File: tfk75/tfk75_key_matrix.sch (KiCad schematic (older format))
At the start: 1 part

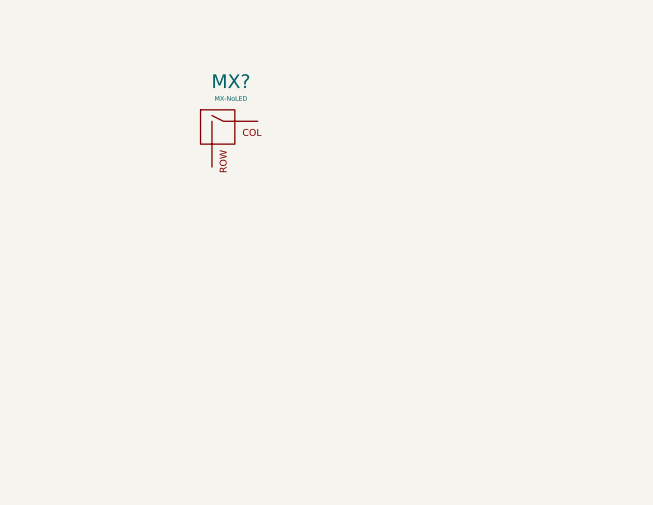
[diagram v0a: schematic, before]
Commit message: Begin key matrix
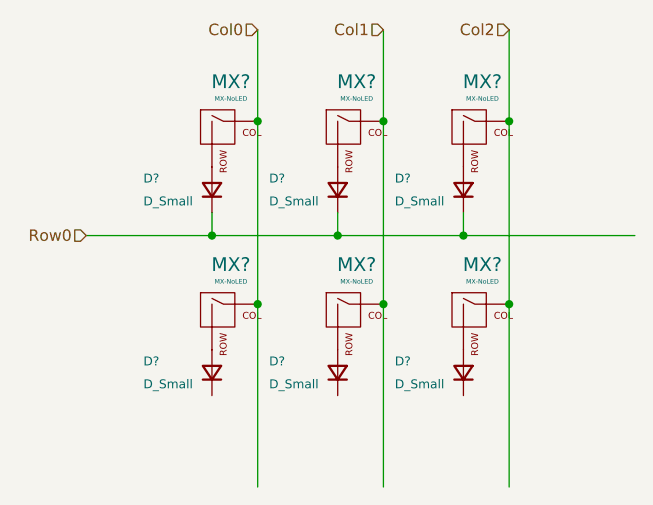
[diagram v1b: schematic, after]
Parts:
- added D? (x6): D_Small, symbol Device:D_Small
- added MX? (x5): MX-NoLED, symbol MX_Alps_Hybrid:MX-NoLED
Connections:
- net labels added: Col0, Col1, Col2, Row0
- wire segments 0 -> 16
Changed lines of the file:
@@
 	1    0    0    -1
 $EndComp
+Wire Wire Line
+	1750 1250 1750 850
+$Comp
+L Device:D_Small D?
+U 1 1 601B104B
+P 1550 1550
+F 0 "D?" V 1600 1850 39  0000 R CNN
+F 1 "D_Small" V 1500 1850 39  0000 R CNN
+F 2 "" V 1550 1550 50  0001 C CNN
+F 3 "~" V 1550 1550 50  0001 C CNN
+	1    1550 1550
+	0    -1   -1   0
+$EndComp
+$Comp
+L MX_Alps_Hybrid:MX-NoLED MX?
+U 1 1 601B478E
+P 2150 1300
+F 0 "MX?" H 2183 1523 60  0000 C CNN
+F 1 "MX-NoLED" H 2183 1449 20  0000 C CNN
+F 2 "" H 1525 1275 60  0001 C CNN
+F 3 "" H 1525 1275 60  0001 C CNN
+	1    2150 1300
+	1    0    0    -1
+$EndComp
+Wire Wire Line
+	2300 1250 2300 850
+$Comp
+L Device:D_Small D?
+U 1 1 601B4795
+P 2100 1550
+F 0 "D?" V 2150 1850 39  0000 R CNN
+F 1 "D_Small" V 2050 1850 39  0000 R CNN
+F 2 "" V 2100 1550 50  0001 C CNN
+F 3 "~" V 2100 1550 50  0001 C CNN
+	1    2100 1550
+	0    -1   -1   0
+$EndComp
+$Comp
+L MX_Alps_Hybrid:MX-NoLED MX?
+U 1 1 601B5B28
+P 2700 1300
+F 0 "MX?" H 2733 1523 60  0000 C CNN
+F 1 "MX-NoLED" H 2733 1449 20  0000 C CNN
+F 2 "" H 2075 1275 60  0001 C CNN
+F 3 "" H 2075 1275 60  0001 C CNN
+	1    2700 1300
+	1    0    0    -1
+$EndComp
+Wire Wire Line
+	2850 1250 2850 850
+$Comp
+L Device:D_Small D?
+U 1 1 601B5B2F
+P 2650 1550
+F 0 "D?" V 2700 1850 39  0000 R CNN
+F 1 "D_Small" V 2600 1850 39  0000 R CNN
+F 2 "" V 2650 1550 50  0001 C CNN
+F 3 "~" V 2650 1550 50  0001 C CNN
+	1    2650 1550
+	0    -1   -1   0
+$EndComp
+Text HLabel 1750 850  0    50   Input ~ 0
+Col0
+Connection ~ 1750 1250
+Wire Wire Line
+	1550 1650 1550 1750
+Wire Wire Line
+	1550 1750 2100 1750
+Wire Wire Line
+	2100 1650 2100 1750
+Connection ~ 2100 1750
+Wire Wire Line
+	2100 1750 2650 1750
+Wire Wire Line
+	2650 1650 2650 1750
+Connection ~ 2650 1750
+Wire Wire Line
+	2650 1750 3400 1750
+Text HLabel 2300 850  0    50   Input ~ 0
+Col1
+Text HLabel 2850 850  0    50   Input ~ 0
+Col2
+Wire Wire Line
+	1550 1750 1000 1750
+Connection ~ 1550 1750
+Text HLabel 1000 1750 0    50   Input ~ 0
+Row0
+$Comp
+L MX_Alps_Hybrid:MX-NoLED MX?
+U 1 1 601C32AD
+P 1600 2100
+F 0 "MX?" H 1633 2323 60  0000 C CNN
+F 1 "MX-NoLED" H 1633 2249 20  0000 C CNN
+F 2 "" H 975 2075 60  0001 C CNN
+F 3 "" H 975 2075 60  0001 C CNN
+	1    1600 2100
+	1    0    0    -1
+$EndComp
+$Comp
+L Device:D_Small D?
+U 1 1 601C32B4
+P 1550 2350
+F 0 "D?" V 1600 2650 39  0000 R CNN
+F 1 "D_Small" V 1500 2650 39  0000 R CNN
+F 2 "" V 1550 2350 50  0001 C CNN
+F 3 "~" V 1550 2350 50  0001 C CNN
+	1    1550 2350
+	0    -1   -1   0
+$EndComp
+$Comp
+L MX_Alps_Hybrid:MX-NoLED MX?
+U 1 1 601C32BA
+P 2150 2100
+F 0 "MX?" H 2183 2323 60  0000 C CNN
+F 1 "MX-NoLED" H 2183 2249 20  0000 C CNN
+F 2 "" H 1525 2075 60  0001 C CNN
+F 3 "" H 1525 2075 60  0001 C CNN
+	1    2150 2100
+	1    0    0    -1
+$EndComp
+$Comp
+L Device:D_Small D?
+U 1 1 601C32C1
+P 2100 2350
+F 0 "D?" V 2150 2650 39  0000 R CNN
+F 1 "D_Small" V 2050 2650 39  0000 R CNN
+F 2 "" V 2100 2350 50  0001 C CNN
+F 3 "~" V 2100 2350 50  0001 C CNN
+	1    2100 2350
+	0    -1   -1   0
+$EndComp
+$Comp
+L MX_Alps_Hybrid:MX-NoLED MX?
+U 1 1 601C32C7
+P 2700 2100
+F 0 "MX?" H 2733 2323 60  0000 C CNN
+F 1 "MX-NoLED" H 2733 2249 20  0000 C CNN
+F 2 "" H 2075 2075 60  0001 C CNN
+F 3 "" H 2075 2075 60  0001 C CNN
+	1    2700 2100
+	1    0    0    -1
+$EndComp
+$Comp
+L Device:D_Small D?
+U 1 1 601C32CE
+P 2650 2350
+F 0 "D?" V 2700 2650 39  0000 R CNN
+F 1 "D_Small" V 2600 2650 39  0000 R CNN
+F 2 "" V 2650 2350 50  0001 C CNN
+F 3 "~" V 2650 2350 50  0001 C CNN
+	1    2650 2350
+	0    -1   -1   0
+$EndComp
+Wire Wire Line
+	1750 2050 1750 2850
+Connection ~ 1750 2050
+Wire Wire Line
+	2300 2050 2300 2850
+Connection ~ 2300 2050
+Wire Wire Line
+	2850 2050 2850 2850
+Connection ~ 2850 2050
+Wire Wire Line
+	1750 1250 1750 2050
+Connection ~ 2300 1250
+Wire Wire Line
+	2850 1250 2850 2050
+Connection ~ 2850 1250
+Wire Wire Line
+	2300 1250 2300 2050
 $EndSCHEMATC

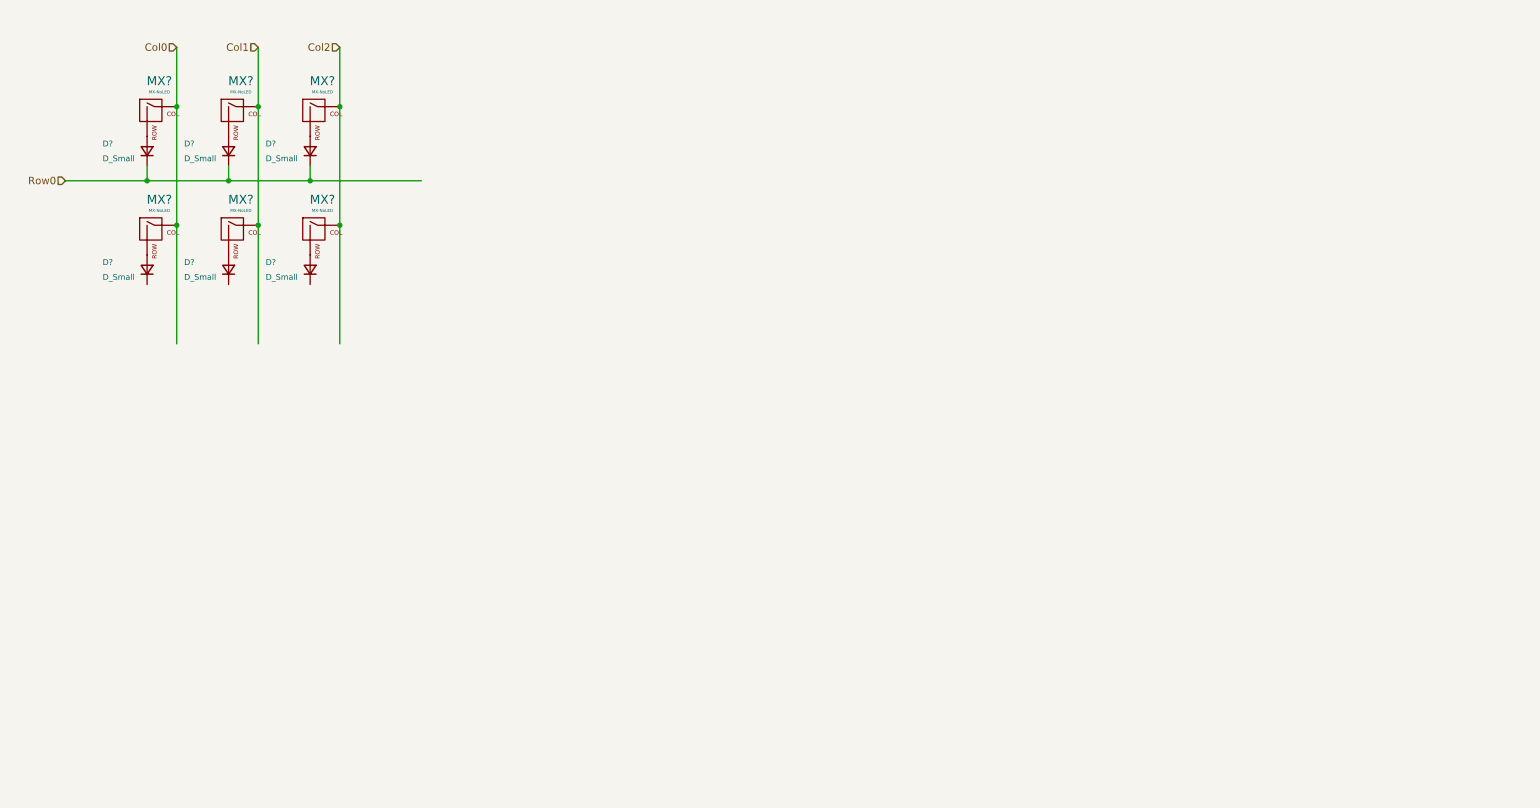
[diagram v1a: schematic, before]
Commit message: Finish key matrix, start reset circuit
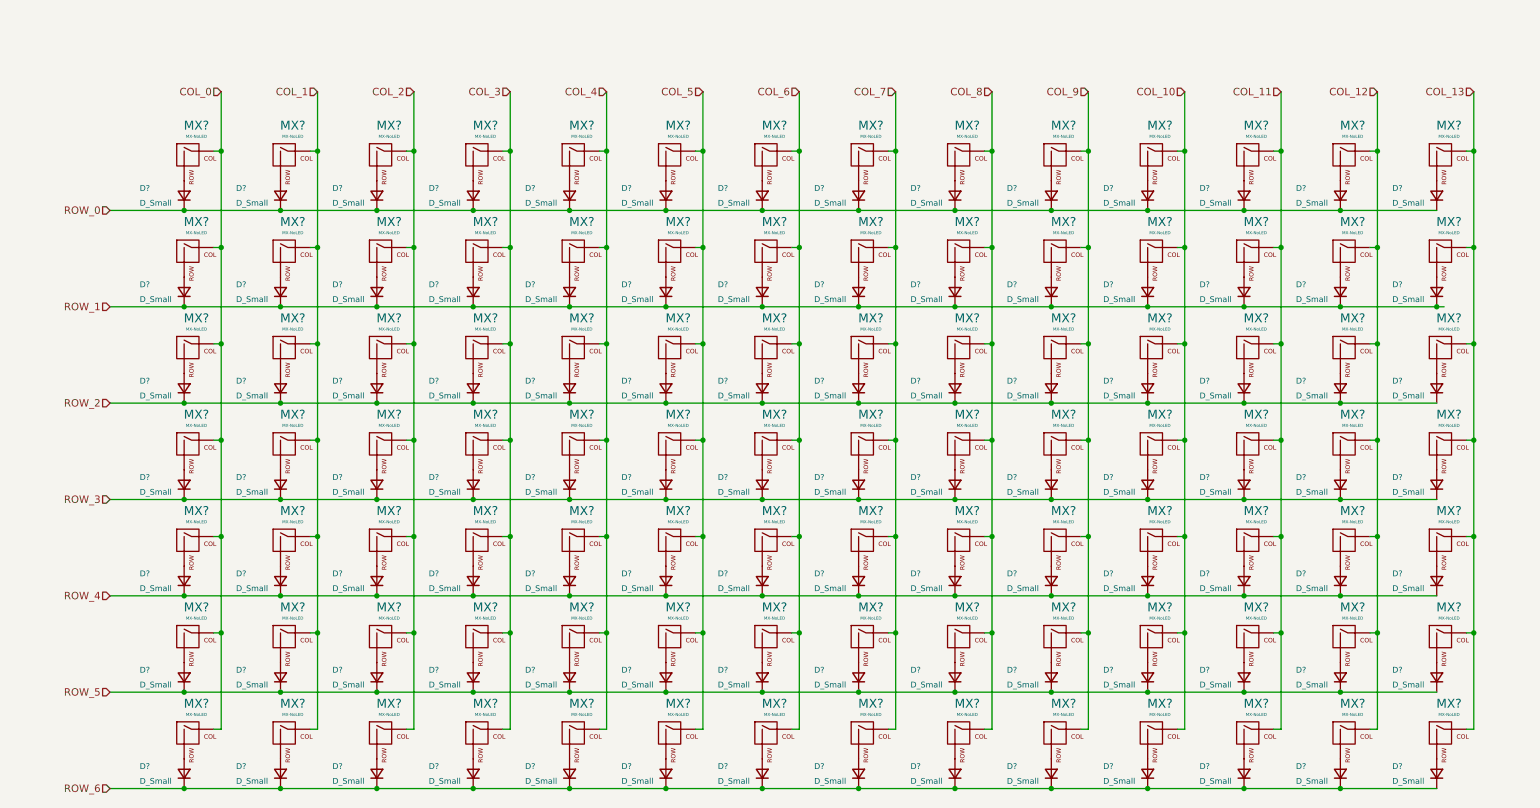
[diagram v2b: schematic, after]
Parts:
- added D? (x92): D_Small, symbol Device:D_Small
- added MX? (x92): MX-NoLED, symbol MX_Alps_Hybrid:MX-NoLED
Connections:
- net labels added: COL_0, COL_1, COL_10, COL_11, COL_12, COL_13, COL_2, COL_3, COL_4, COL_5, COL_6, COL_7, COL_8, COL_9, ROW_0, ROW_1, ROW_2, ROW_3, ROW_4, ROW_5, ROW_6
- net labels removed: Col0, Col1, Col2, Row0
- wire segments 16 -> 295
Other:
- moved on the sheet: D?, MX?

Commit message: Begin RGB matrix
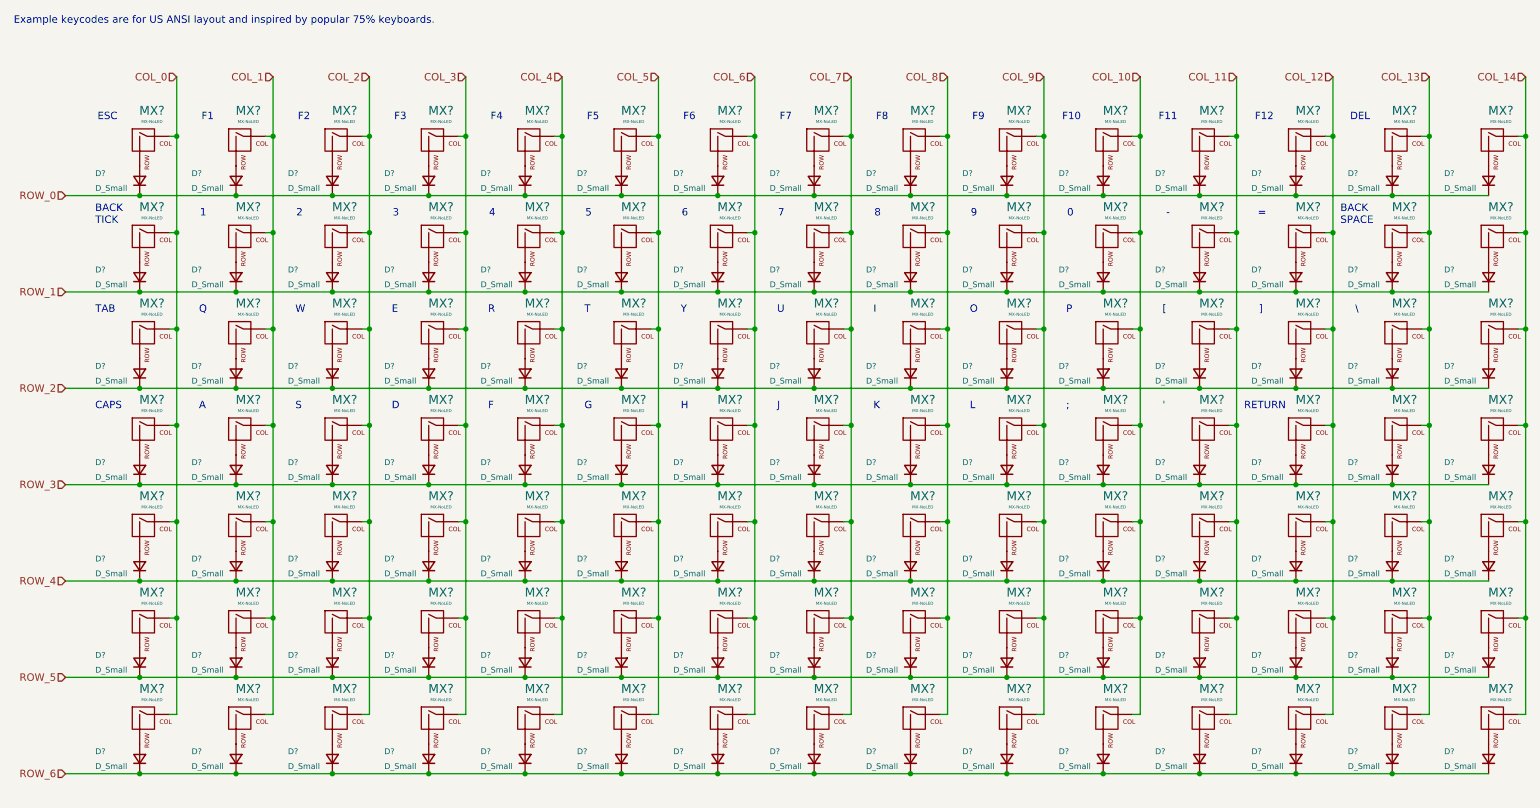
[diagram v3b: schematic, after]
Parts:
- added D? (x7): D_Small, symbol Device:D_Small
- added MX? (x7): MX-NoLED, symbol MX_Alps_Hybrid:MX-NoLED
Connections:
- net ROW_0: now also D?.1 (K)
- net ROW_1: now also D?.1 (K)
- net ROW_2: now also D?.1 (K)
- net ROW_3: now also D?.1 (K)
- net ROW_4: now also D?.1 (K)
- net ROW_5: now also D?.1 (K)
- net ROW_6: now also D?.1 (K)
- new net: D?.2 (A), MX?.2 (ROW) (x7)
- new net COL_14: MX?.1 (COL), MX?.1 (COL), MX?.1 (COL), MX?.1 (COL), MX?.1 (COL), MX?.1 (COL), MX?.1 (COL)
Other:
- note added: "'"
- note added: "-"
- note added: "0"
- note added: "1"
- note added: "2"
- note added: "3"
- note added: "4"
- note added: "5"
- note added: "6"
- note added: "7"
- note added: "8"
- note added: "9"
- note added: ";"
- note added: "="
- note added: "A"
- note added: "BACK\nSPACE"
- note added: "BACK\nTICK"
- note added: "CAPS"
- note added: "D"
- note added: "DEL"
- note added: "E"
- note added: "ESC"
- note added: "Example keycodes are for US ANSI layout and inspired by popular 75% keyboards."
- note added: "F"
- note added: "F1"
- note added: "F10"
- note added: "F11"
- note added: "F12"
- note added: "F2"
- note added: "F3"
- note added: "F4"
- note added: "F5"
- note added: "F6"
- note added: "F7"
- note added: "F8"
- note added: "F9"
- note added: "G"
- note added: "H"
- note added: "I"
- note added: "J"
- note added: "K"
- note added: "L"
- note added: "O"
- note added: "P"
- note added: "Q"
- note added: "R"
- note added: "RETURN"
- note added: "S"
- note added: "T"
- note added: "TAB"
- note added: "U"
- note added: "W"
- note added: "Y"
- note added: "["
- note added: "\"
- note added: "]"
- moved on the sheet: D?, MX?
